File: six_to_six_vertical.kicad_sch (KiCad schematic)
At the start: 12 parts, among them J1 sma, J10 RF Conn, J11 RF Conn, J12 RF Conn, J2 sma, J3 sma, J4 sma, J5 sma, J6 sma, J7 RF Conn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

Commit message: renumber connectors
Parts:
- J10: renamed from J4; value sma -> bnc
- J11: renamed from J5; value sma -> bnc
- J12: renamed from J6; value sma -> bnc
- J7: renamed from J1; value sma -> bnc
- J8: renamed from J2; value sma -> bnc
- J9: renamed from J3; value sma -> bnc
- renumbered J7 to J1, J8 to J2, J9 to J3, J10 to J4, J11 to J5, J12 to J6
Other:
- note added: "2600 mils space between J1 and J2 3900 mils is vertical plate width 1250 mils is distance between two rf plates"
- note removed: "2600 mils space between two j1 650 mils space between two sma on vertikal plate 3900 mils is vertical plate width 1250 mils is distance between two rf plates"
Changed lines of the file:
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@@
     (stroke (width 0) (type default) (color 0 0 0 0))
   )
-  (text "2600 mils space between two j1\n 650 mils space between two sma on vertikal plate\n3900 mils is vertical plate width\n1250 mils is distance between two rf plates"
+  (text "2600 mils space between J1 and J2\n3900 mils is vertical plate width\n1250 mils is distance between two rf plates"
     (at 106.68 38.1 0)
     (effects (font (size 1.27 1.27)) (justify left bottom))
@@
   (symbol (lib_id "Connector:Conn_Coaxial") (at 77.47 87.63 0) (mirror y) (unit 1)
     (in_bom yes) (on_board yes)
-    (property "Reference" "J3" (id 0) (at 77.7874 80.01 0))
-    (property "Value" "sma" (id 1) (at 77.7874 82.55 0))
+    (property "Reference" "J9" (id 0) (at 77.7874 80.01 0))
+    (property "Value" "bnc" (id 1) (at 77.7874 82.55 0))
     (property "Footprint" "Library:BNC_vertical" (id 2) (at 77.47 87.63 0)
       (effects (font (size 1.27 1.27)) hide)
@@
   (symbol (lib_id "Connector:Conn_Coaxial") (at 77.47 106.68 0) (mirror y) (unit 1)
     (in_bom yes) (on_board yes)
-    (property "Reference" "J4" (id 0) (at 77.7874 99.06 0))
-    (property "Value" "sma" (id 1) (at 77.7874 101.6 0))
+    (property "Reference" "J10" (id 0) (at 77.7874 99.06 0))
+    (property "Value" "bnc" (id 1) (at 77.7874 101.6 0))
     (property "Footprint" "Library:BNC_vertical" (id 2) (at 77.47 106.68 0)
       (effects (font (size 1.27 1.27)) hide)
@@
   (symbol (lib_id "Connector_Generic:Conn_02x06_Odd_Even") (at 118.11 81.28 0) (unit 1)
     (in_bom yes) (on_board yes) (fields_autoplaced)
-    (property "Reference" "J7" (id 0) (at 119.38 69.85 0))
+    (property "Reference" "J1" (id 0) (at 119.38 69.85 0))
     (property "Value" "RF Conn" (id 1) (at 119.38 72.39 0))
     (property "Footprint" "Connector_PinSocket_2.54mm:PinSocket_2x06_P2.54mm_Vertical" (id 2) (at 118.11 81.28 0)
@@
   (symbol (lib_id "Connector_Generic:Conn_02x06_Odd_Even") (at 143.51 81.28 0) (unit 1)
     (in_bom yes) (on_board yes) (fields_autoplaced)
-    (property "Reference" "J9" (id 0) (at 144.78 69.85 0))
+    (property "Reference" "J3" (id 0) (at 144.78 69.85 0))
     (property "Value" "RF Conn" (id 1) (at 144.78 72.39 0))
     (property "Footprint" "Connector_PinSocket_2.54mm:PinSocket_2x06_P2.54mm_Vertical" (id 2) (at 143.51 81.28 0)
@@
   (symbol (lib_id "Connector_Generic:Conn_02x06_Odd_Even") (at 143.51 109.22 0) (unit 1)
     (in_bom yes) (on_board yes) (fields_autoplaced)
-    (property "Reference" "J10" (id 0) (at 144.78 97.79 0))
+    (property "Reference" "J4" (id 0) (at 144.78 97.79 0))
     (property "Value" "RF Conn" (id 1) (at 144.78 100.33 0))
     (property "Footprint" "Connector_PinSocket_2.54mm:PinSocket_2x06_P2.54mm_Vertical" (id 2) (at 143.51 109.22 0)
@@
   (symbol (lib_id "Connector:Conn_Coaxial") (at 77.47 127 0) (mirror y) (unit 1)
     (in_bom yes) (on_board yes)
-    (property "Reference" "J5" (id 0) (at 77.7874 119.38 0))
-    (property "Value" "sma" (id 1) (at 77.7874 121.92 0))
+    (property "Reference" "J11" (id 0) (at 77.7874 119.38 0))
+    (property "Value" "bnc" (id 1) (at 77.7874 121.92 0))
     (property "Footprint" "Library:BNC_vertical" (id 2) (at 77.47 127 0)
       (effects (font (size 1.27 1.27)) hide)
@@
   (symbol (lib_id "Connector_Generic:Conn_02x06_Odd_Even") (at 168.91 109.22 0) (unit 1)
     (in_bom yes) (on_board yes) (fields_autoplaced)
-    (property "Reference" "J12" (id 0) (at 170.18 97.79 0))
+    (property "Reference" "J6" (id 0) (at 170.18 97.79 0))
     (property "Value" "RF Conn" (id 1) (at 170.18 100.33 0))
     (property "Footprint" "Connector_PinSocket_2.54mm:PinSocket_2x06_P2.54mm_Vertical" (id 2) (at 168.91 109.22 0)
@@
   (symbol (lib_id "Connector:Conn_Coaxial") (at 77.47 67.31 0) (mirror y) (unit 1)
     (in_bom yes) (on_board yes)
-    (property "Reference" "J2" (id 0) (at 77.7874 59.69 0))
-    (property "Value" "sma" (id 1) (at 77.7874 62.23 0))
+    (property "Reference" "J8" (id 0) (at 77.7874 59.69 0))
+    (property "Value" "bnc" (id 1) (at 77.7874 62.23 0))
     (property "Footprint" "Library:BNC_vertical" (id 2) (at 77.47 67.31 0)
       (effects (font (size 1.27 1.27)) hide)
@@
   (symbol (lib_id "Connector_Generic:Conn_02x06_Odd_Even") (at 118.11 109.22 0) (unit 1)
     (in_bom yes) (on_board yes) (fields_autoplaced)
-    (property "Reference" "J8" (id 0) (at 119.38 97.79 0))
+    (property "Reference" "J2" (id 0) (at 119.38 97.79 0))
     (property "Value" "RF Conn" (id 1) (at 119.38 100.33 0))
     (property "Footprint" "Connector_PinSocket_2.54mm:PinSocket_2x06_P2.54mm_Vertical" (id 2) (at 118.11 109.22 0)
@@
   (symbol (lib_id "Connector_Generic:Conn_02x06_Odd_Even") (at 168.91 81.28 0) (unit 1)
     (in_bom yes) (on_board yes) (fields_autoplaced)
-    (property "Reference" "J11" (id 0) (at 170.18 69.85 0))
+    (property "Reference" "J5" (id 0) (at 170.18 69.85 0))
     (property "Value" "RF Conn" (id 1) (at 170.18 72.39 0))
     (property "Footprint" "Connector_PinSocket_2.54mm:PinSocket_2x06_P2.54mm_Vertical" (id 2) (at 168.91 81.28 0)
@@
   (symbol (lib_id "Connector:Conn_Coaxial") (at 77.47 146.05 0) (mirror y) (unit 1)
     (in_bom yes) (on_board yes)
-    (property "Reference" "J6" (id 0) (at 77.7874 138.43 0))
-    (property "Value" "sma" (id 1) (at 77.7874 140.97 0))
+    (property "Reference" "J12" (id 0) (at 77.7874 138.43 0))
+    (property "Value" "bnc" (id 1) (at 77.7874 140.97 0))
     (property "Footprint" "Library:BNC_vertical" (id 2) (at 77.47 146.05 0)
       (effects (font (size 1.27 1.27)) hide)
@@
   (symbol (lib_id "Connector:Conn_Coaxial") (at 77.47 48.26 0) (mirror y) (unit 1)
     (in_bom yes) (on_board yes)
-    (property "Reference" "J1" (id 0) (at 77.7874 40.64 0))
-    (property "Value" "sma" (id 1) (at 77.7874 43.18 0))
+    (property "Reference" "J7" (id 0) (at 77.7874 40.64 0))
+    (property "Value" "bnc" (id 1) (at 77.7874 43.18 0))
     (property "Footprint" "Library:BNC_vertical" (id 2) (at 77.47 48.26 0)
       (effects (font (size 1.27 1.27)) hide)
@@
       (reference "#PWR0101") (unit 1) (value "GND") (footprint "")
     )
+    (path "/368a52e7-409b-4b3e-baa8-44243f07ee94"
+      (reference "J1") (unit 1) (value "RF Conn") (footprint "Connector_PinSocket_2.54mm:PinSocket_2x06_P2.54mm_Vertical")
+    )
+    (path "/a0f9eb9e-6261-46fa-9db7-f79e9e1a9f78"
+      (reference "J2") (unit 1) (value "RF Conn") (footprint "Connector_PinSocket_2.54mm:PinSocket_2x06_P2.54mm_Vertical")
+    )
+    (path "/37dbb3b8-43ed-4a83-b51d-064fb1956ebc"
+      (reference "J3") (unit 1) (value "RF Conn") (footprint "Connector_PinSocket_2.54mm:PinSocket_2x06_P2.54mm_Vertical")
+    )
+    (path "/3d59945f-c395-4bce-81e5-20c72f466186"
+      (reference "J4") (unit 1) (value "RF Conn") (footprint "Connector_PinSocket_2.54mm:PinSocket_2x06_P2.54mm_Vertical")
+    )
+    (path "/a89f80bd-a7f9-4c43-a98f-a55cf85e5b2a"
+      (reference "J5") (unit 1) (value "RF Conn") (footprint "Connector_PinSocket_2.54mm:PinSocket_2x06_P2.54mm_Vertical")
+    )
+    (path "/45503cb2-b4dc-445b-aa83-b8ea95c2ac4e"
+      (reference "J6") (unit 1) (value "RF Conn") (footprint "Connector_PinSocket_2.54mm:PinSocket_2x06_P2.54mm_Vertical")
+    )
     (path "/c57411a0-864a-4a64-bac5-c84641c1d89d"
-      (reference "J1") (unit 1) (value "sma") (footprint "Library:BNC_vertical")
+      (reference "J7") (unit 1) (value "bnc") (footprint "Library:BNC_vertical")
     )
     (path "/55d32049-557b-4bb4-9a57-13b17a68677a"
-      (reference "J2") (unit 1) (value "sma") (footprint "Library:BNC_vertical")
+      (reference "J8") (unit 1) (value "bnc") (footprint "Library:BNC_vertical")
     )
     (path "/127267ed-50af-4930-a36d-aa7f2d722516"
-      (reference "J3") (unit 1) (value "sma") (footprint "Library:BNC_vertical")
+      (reference "J9") (unit 1) (value "bnc") (footprint "Library:BNC_vertical")
     )
     (path "/2417e7c1-898d-4de5-8c65-cf7f18f22bf3"
-      (reference "J4") (unit 1) (value "sma") (footprint "Library:BNC_vertical")
+      (reference "J10") (unit 1) (value "bnc") (footprint "Library:BNC_vertical")
     )
     (path "/42358dba-dd22-491b-856d-a777cab0024c"
-      (reference "J5") (unit 1) (value "sma") (footprint "Library:BNC_vertical")
+      (reference "J11") (unit 1) (value "bnc") (footprint "Library:BNC_vertical")
     )
     (path "/ae979820-55e5-4570-a373-e9186357c947"
-      (reference "J6") (unit 1) (value "sma") (footprint "Library:BNC_vertical")
-    )
-    (path "/368a52e7-409b-4b3e-baa8-44243f07ee94"
-      (reference "J7") (unit 1) (value "RF Conn") (footprint "Connector_PinSocket_2.54mm:PinSocket_2x06_P2.54mm_Vertical")
-    )
-    (path "/a0f9eb9e-6261-46fa-9db7-f79e9e1a9f78"
-      (reference "J8") (unit 1) (value "RF Conn") (footprint "Connector_PinSocket_2.54mm:PinSocket_2x06_P2.54mm_Vertical")
-    )
-    (path "/37dbb3b8-43ed-4a83-b51d-064fb1956ebc"
-      (reference "J9") (unit 1) (value "RF Conn") (footprint "Connector_PinSocket_2.54mm:PinSocket_2x06_P2.54mm_Vertical")
-    )
-    (path "/3d59945f-c395-4bce-81e5-20c72f466186"
-      (reference "J10") (unit 1) (value "RF Conn") (footprint "Connector_PinSocket_2.54mm:PinSocket_2x06_P2.54mm_Vertical")
-    )
-    (path "/a89f80bd-a7f9-4c43-a98f-a55cf85e5b2a"
-      (reference "J11") (unit 1) (value "RF Conn") (footprint "Connector_PinSocket_2.54mm:PinSocket_2x06_P2.54mm_Vertical")
-    )
-    (path "/45503cb2-b4dc-445b-aa83-b8ea95c2ac4e"
-      (reference "J12") (unit 1) (value "RF Conn") (footprint "Connector_PinSocket_2.54mm:PinSocket_2x06_P2.54mm_Vertical")
-    )
-  )
+      (reference "J12") (unit 1) (value "bnc") (footprint "Library:BNC_vertical")
+    )
+  )

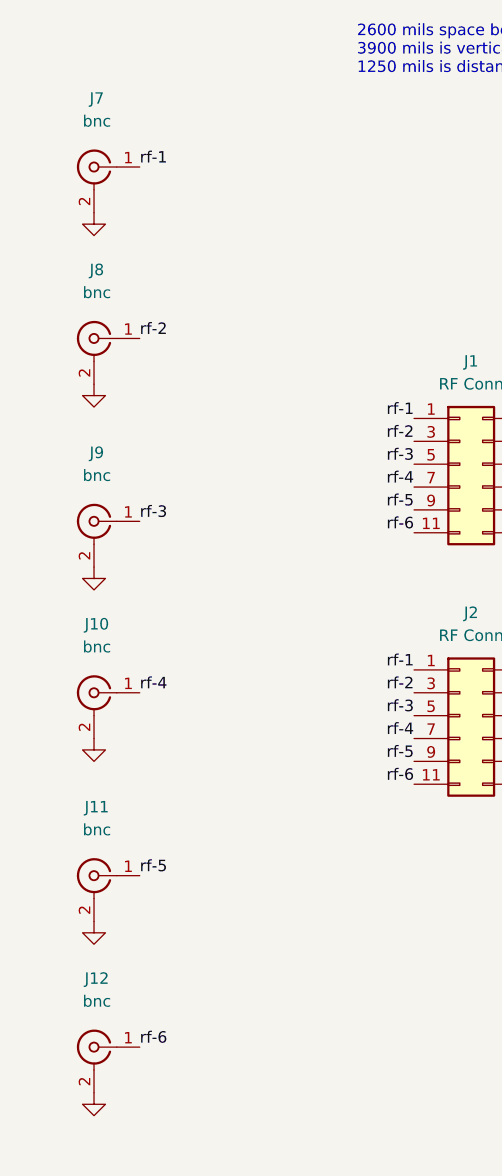
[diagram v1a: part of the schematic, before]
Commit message: added BNC part number
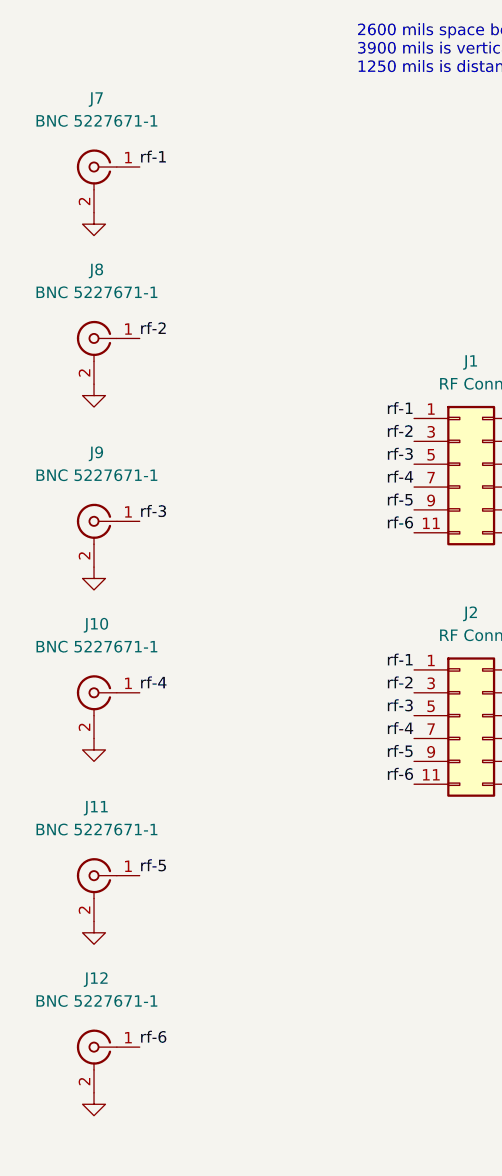
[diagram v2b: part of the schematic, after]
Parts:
- J10, J11, J12, J7, J8, J9: value bnc -> BNC 5227671-1
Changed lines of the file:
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@@
     (in_bom yes) (on_board yes)
     (property "Reference" "J9" (id 0) (at 77.7874 80.01 0))
-    (property "Value" "bnc" (id 1) (at 77.7874 82.55 0))
+    (property "Value" "BNC 5227671-1" (id 1) (at 77.7874 82.55 0))
     (property "Footprint" "Library:BNC_vertical" (id 2) (at 77.47 87.63 0)
       (effects (font (size 1.27 1.27)) hide)
     )
-    (property "Datasheet" " ~" (id 3) (at 77.47 87.63 0)
+    (property "Datasheet" "https://www.te.com/commerce/DocumentDelivery/DDEController?Action=srchrtrv&DocNm=5227671&DocType=Customer+Drawing&DocLang=English&DocFormat=pdf&PartCntxt=5227671-1" (id 3) (at 77.47 87.63 0)
       (effects (font (size 1.27 1.27)) hide)
     )
@@
     (in_bom yes) (on_board yes)
     (property "Reference" "J10" (id 0) (at 77.7874 99.06 0))
-    (property "Value" "bnc" (id 1) (at 77.7874 101.6 0))
+    (property "Value" "BNC 5227671-1" (id 1) (at 77.7874 101.6 0))
     (property "Footprint" "Library:BNC_vertical" (id 2) (at 77.47 106.68 0)
       (effects (font (size 1.27 1.27)) hide)
     )
-    (property "Datasheet" " ~" (id 3) (at 77.47 106.68 0)
+    (property "Datasheet" "https://www.te.com/commerce/DocumentDelivery/DDEController?Action=srchrtrv&DocNm=5227671&DocType=Customer+Drawing&DocLang=English&DocFormat=pdf&PartCntxt=5227671-1" (id 3) (at 77.47 106.68 0)
       (effects (font (size 1.27 1.27)) hide)
     )
@@
     (in_bom yes) (on_board yes)
     (property "Reference" "J11" (id 0) (at 77.7874 119.38 0))
-    (property "Value" "bnc" (id 1) (at 77.7874 121.92 0))
+    (property "Value" "BNC 5227671-1" (id 1) (at 77.7874 121.92 0))
     (property "Footprint" "Library:BNC_vertical" (id 2) (at 77.47 127 0)
       (effects (font (size 1.27 1.27)) hide)
     )
-    (property "Datasheet" " ~" (id 3) (at 77.47 127 0)
+    (property "Datasheet" "https://www.te.com/commerce/DocumentDelivery/DDEController?Action=srchrtrv&DocNm=5227671&DocType=Customer+Drawing&DocLang=English&DocFormat=pdf&PartCntxt=5227671-1" (id 3) (at 77.47 127 0)
       (effects (font (size 1.27 1.27)) hide)
     )
@@
     (in_bom yes) (on_board yes)
     (property "Reference" "J8" (id 0) (at 77.7874 59.69 0))
-    (property "Value" "bnc" (id 1) (at 77.7874 62.23 0))
+    (property "Value" "BNC 5227671-1" (id 1) (at 77.7874 62.23 0))
     (property "Footprint" "Library:BNC_vertical" (id 2) (at 77.47 67.31 0)
       (effects (font (size 1.27 1.27)) hide)
     )
-    (property "Datasheet" " ~" (id 3) (at 77.47 67.31 0)
+    (property "Datasheet" "https://www.te.com/commerce/DocumentDelivery/DDEController?Action=srchrtrv&DocNm=5227671&DocType=Customer+Drawing&DocLang=English&DocFormat=pdf&PartCntxt=5227671-1" (id 3) (at 77.47 67.31 0)
       (effects (font (size 1.27 1.27)) hide)
     )
@@
     (in_bom yes) (on_board yes)
     (property "Reference" "J12" (id 0) (at 77.7874 138.43 0))
-    (property "Value" "bnc" (id 1) (at 77.7874 140.97 0))
+    (property "Value" "BNC 5227671-1" (id 1) (at 77.7874 140.97 0))
     (property "Footprint" "Library:BNC_vertical" (id 2) (at 77.47 146.05 0)
       (effects (font (size 1.27 1.27)) hide)
     )
-    (property "Datasheet" " ~" (id 3) (at 77.47 146.05 0)
+    (property "Datasheet" "https://www.te.com/commerce/DocumentDelivery/DDEController?Action=srchrtrv&DocNm=5227671&DocType=Customer+Drawing&DocLang=English&DocFormat=pdf&PartCntxt=5227671-1" (id 3) (at 77.47 146.05 0)
       (effects (font (size 1.27 1.27)) hide)
     )
@@
     (in_bom yes) (on_board yes)
     (property "Reference" "J7" (id 0) (at 77.7874 40.64 0))
-    (property "Value" "bnc" (id 1) (at 77.7874 43.18 0))
+    (property "Value" "BNC 5227671-1" (id 1) (at 77.7874 43.18 0))
     (property "Footprint" "Library:BNC_vertical" (id 2) (at 77.47 48.26 0)
       (effects (font (size 1.27 1.27)) hide)
     )
-    (property "Datasheet" " ~" (id 3) (at 77.47 48.26 0)
+    (property "Datasheet" "https://www.te.com/commerce/DocumentDelivery/DDEController?Action=srchrtrv&DocNm=5227671&DocType=Customer+Drawing&DocLang=English&DocFormat=pdf&PartCntxt=5227671-1" (id 3) (at 77.47 48.26 0)
       (effects (font (size 1.27 1.27)) hide)
     )
@@
     )
     (path "/c57411a0-864a-4a64-bac5-c84641c1d89d"
-      (reference "J7") (unit 1) (value "bnc") (footprint "Library:BNC_vertical")
+      (reference "J7") (unit 1) (value "BNC 5227671-1") (footprint "Library:BNC_vertical")
     )
     (path "/55d32049-557b-4bb4-9a57-13b17a68677a"
-      (reference "J8") (unit 1) (value "bnc") (footprint "Library:BNC_vertical")
+      (reference "J8") (unit 1) (value "BNC 5227671-1") (footprint "Library:BNC_vertical")
     )
     (path "/127267ed-50af-4930-a36d-aa7f2d722516"
-      (reference "J9") (unit 1) (value "bnc") (footprint "Library:BNC_vertical")
+      (reference "J9") (unit 1) (value "BNC 5227671-1") (footprint "Library:BNC_vertical")
     )
     (path "/2417e7c1-898d-4de5-8c65-cf7f18f22bf3"
-      (reference "J10") (unit 1) (value "bnc") (footprint "Library:BNC_vertical")
+      (reference "J10") (unit 1) (value "BNC 5227671-1") (footprint "Library:BNC_vertical")
     )
     (path "/42358dba-dd22-491b-856d-a777cab0024c"
-      (reference "J11") (unit 1) (value "bnc") (footprint "Library:BNC_vertical")
+      (reference "J11") (unit 1) (value "BNC 5227671-1") (footprint "Library:BNC_vertical")
     )
     (path "/ae979820-55e5-4570-a373-e9186357c947"
-      (reference "J12") (unit 1) (value "bnc") (footprint "Library:BNC_vertical")
-    )
-  )
+      (reference "J12") (unit 1) (value "BNC 5227671-1") (footprint "Library:BNC_vertical")
+    )
+  )
